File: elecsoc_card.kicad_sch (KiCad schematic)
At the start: 23 parts, among them J1 Conn_01x02_Pin, U1 NA555D

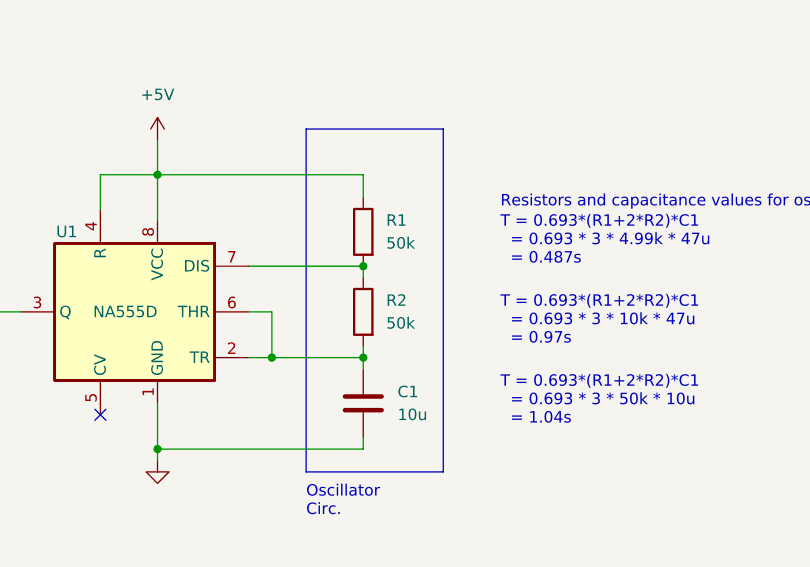
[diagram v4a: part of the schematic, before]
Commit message: Caps added and resistors changed
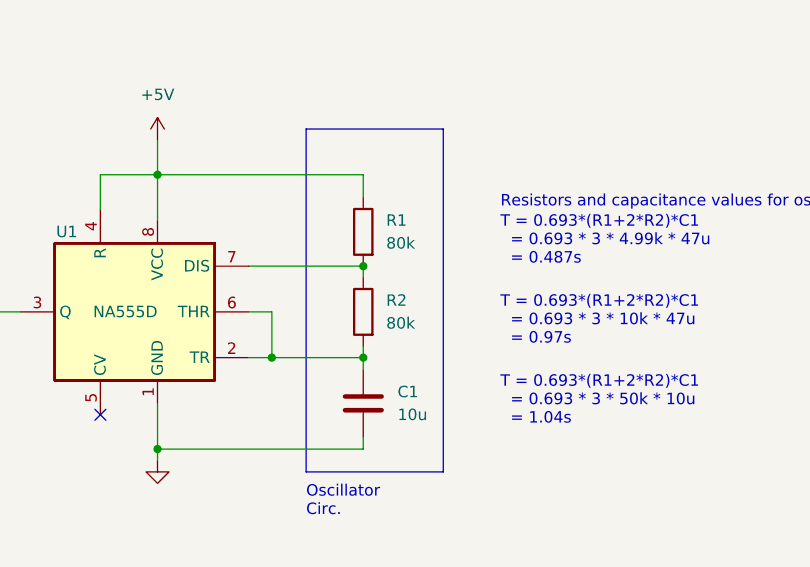
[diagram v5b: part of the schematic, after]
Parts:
- D6, D7: Mfr. No. (none) -> IN-S85AT5UW
- R1, R2: value 50k -> 80k
- U1: Mfr. No: (none) -> 621-NE555S-13
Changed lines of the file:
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@@
+      (effects (font (size 1.27 1.27)) hide)
+    )
+    (property "Mfr. No:" "621-NE555S-13" (at 156.21 91.44 0)
       (effects (font (size 1.27 1.27)) hide)
     )
@@
       (effects (font (size 1.27 1.27)) hide)
     )
-    (property "Datasheet" "~" (at 111.76 99.06 0)
+    (property "Datasheet" "https://www.mouser.ie/datasheet/2/180/IN_S85AT_Series_V1_1-2323391.pdf" (at 111.76 99.06 0)
+      (effects (font (size 1.27 1.27)) hide)
+    )
+    (property "Mfr. No." "IN-S85AT5UW" (at 111.76 99.06 90)
       (effects (font (size 1.27 1.27)) hide)
     )
@@
       (effects (font (size 1.27 1.27)) hide)
     )
-    (property "Datasheet" "~" (at 102.87 99.06 0)
+    (property "Datasheet" "https://www.mouser.ie/datasheet/2/180/IN_S85AT_Series_V1_1-2323391.pdf" (at 102.87 99.06 0)
+      (effects (font (size 1.27 1.27)) hide)
+    )
+    (property "Mfr. No." "IN-S85AT5UW" (at 102.87 99.06 90)
       (effects (font (size 1.27 1.27)) hide)
     )
@@
       (effects (font (size 1.27 1.27)) hide)
     )
-    (property "Datasheet" "~" (at 191.77 38.1 0)
+    (property "Datasheet" "https://www.mouser.ie/datasheet/2/281/1/GRT155D70G106ME13_01A-3135786.pdf" (at 191.77 38.1 0)
       (effects (font (size 1.27 1.27)) hide)
     )
@@
       (effects (font (size 1.27 1.27)) hide)
     )
-    (property "Datasheet" "~" (at 181.61 101.6 0)
+    (property "Datasheet" "https://www.mouser.ie/datasheet/2/281/1/GRT155D70G106ME13_01A-3135786.pdf" (at 181.61 101.6 0)
       (effects (font (size 1.27 1.27)) hide)
     )
@@
       (effects (font (size 1.27 1.27)) (justify right))
     )
-    (property "Value" "50k" (at 184.15 92.71 0)
+    (property "Value" "80k" (at 184.15 92.71 0)
       (effects (font (size 1.27 1.27)) (justify right))
     )
@@
       (effects (font (size 1.27 1.27)) (justify right))
     )
-    (property "Value" "50k" (at 184.15 83.82 0)
-      (effects (font (size 1.27 1.27)) (justify right))
-    )
+    (property "Value" "80k" (at 184.15 83.82 0)
+      (effects (font (size 1.27 1.27)) (justify right))
+    )

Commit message: Changed resistors
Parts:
- D1, D2, D3, D5: Mfr. No. (none) -> SMLMN2WB1CW1
- D4: Mfr. No (none) -> SMLMN2WB1CW1
- R3, R4, R5, R6, R7: value 390 -> 3k
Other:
- note added: "RED Leds Vf = 3V If = 5mA Rled = (Vs - Vf)/If = (5 - 3)/0.005 = 400 White Leds Vf = 2.9 If = 5m Rled = (Vs - Vf)/If = (5 - 2.9)/0.005 = 420"
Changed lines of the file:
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@@
+    (effects (font (size 1.27 1.27)) (justify left bottom))
+  )
+  (text "RED Leds\nVf = 3V\nIf = 5mA\nRled = (Vs - Vf)/If = (5 - 3)/0.005 = 400\n\nWhite Leds\nVf = 2.9\nIf = 5m\nRled = (Vs - Vf)/If = (5 - 2.9)/0.005 = 420"
+    (at 195.58 124.46 0)
     (effects (font (size 1.27 1.27)) (justify left bottom))
   )
@@
   )
   (symbol (lib_id "Device:R") (at 120.65 71.12 0) (mirror y) (unit 1)
-    (in_bom yes) (on_board yes) (dnp no) (fields_autoplaced)
-    (property "Reference" "R3" (at 118.11 70.485 0)
-      (effects (font (size 1.27 1.27)) (justify left))
-    )
-    (property "Value" "390" (at 118.11 73.025 0)
+    (in_bom yes) (on_board yes) (dnp no)
+    (property "Reference" "R3" (at 115.57 69.85 0)
+      (effects (font (size 1.27 1.27)) (justify right))
+    )
+    (property "Value" "3k" (at 118.11 73.025 0) (do_not_autoplace)
       (effects (font (size 1.27 1.27)) (justify left))
     )
@@
     )
     (property "Datasheet" "~" (at 111.76 82.55 0)
+      (effects (font (size 1.27 1.27)) hide)
+    )
+    (property "Mfr. No." "SMLMN2WB1CW1 " (at 111.76 82.55 90)
       (effects (font (size 1.27 1.27)) hide)
     )
@@
   )
   (symbol (lib_id "Device:R") (at 102.87 71.12 0) (mirror y) (unit 1)
-    (in_bom yes) (on_board yes) (dnp no) (fields_autoplaced)
-    (property "Reference" "R5" (at 100.33 70.485 0)
-      (effects (font (size 1.27 1.27)) (justify left))
-    )
-    (property "Value" "390" (at 100.33 73.025 0)
+    (in_bom yes) (on_board yes) (dnp no)
+    (property "Reference" "R5" (at 97.79 69.85 0)
+      (effects (font (size 1.27 1.27)) (justify right))
+    )
+    (property "Value" "3k" (at 100.33 73.025 0) (do_not_autoplace)
       (effects (font (size 1.27 1.27)) (justify left))
     )
@@
       (effects (font (size 1.27 1.27)) hide)
     )
+    (property "Mfr. No." "SMLMN2WB1CW1 " (at 120.65 82.55 90)
+      (effects (font (size 1.27 1.27)) hide)
+    )
     (pin "1")
     (pin "2")
@@
   )
   (symbol (lib_id "Device:R") (at 93.98 71.12 0) (mirror y) (unit 1)
-    (in_bom yes) (on_board yes) (dnp no) (fields_autoplaced)
-    (property "Reference" "R6" (at 91.44 70.485 0)
-      (effects (font (size 1.27 1.27)) (justify left))
-    )
-    (property "Value" "390" (at 91.44 73.025 0)
+    (in_bom yes) (on_board yes) (dnp no)
+    (property "Reference" "R6" (at 88.9 69.85 0)
+      (effects (font (size 1.27 1.27)) (justify right))
+    )
+    (property "Value" "3k" (at 91.44 73.025 0) (do_not_autoplace)
       (effects (font (size 1.27 1.27)) (justify left))
     )
@@
       (effects (font (size 1.27 1.27)) hide)
     )
+    (property "Mfr. No" "SMLMN2WB1CW1 " (at 93.98 82.55 90)
+      (effects (font (size 1.27 1.27)) hide)
+    )
     (pin "1")
     (pin "2")
@@
       (effects (font (size 1.27 1.27)) hide)
     )
+    (property "Mfr. No." "SMLMN2WB1CW1 " (at 102.87 82.55 90)
+      (effects (font (size 1.27 1.27)) hide)
+    )
     (pin "1")
     (pin "2")
@@
   )
   (symbol (lib_id "Device:R") (at 85.09 71.12 0) (mirror y) (unit 1)
-    (in_bom yes) (on_board yes) (dnp no) (fields_autoplaced)
+    (in_bom yes) (on_board yes) (dnp no)
     (property "Reference" "R7" (at 82.55 70.485 0)
       (effects (font (size 1.27 1.27)) (justify left))
     )
-    (property "Value" "390" (at 82.55 73.025 0)
+    (property "Value" "3k" (at 82.55 73.025 0) (do_not_autoplace)
       (effects (font (size 1.27 1.27)) (justify left))
     )
@@
   )
   (symbol (lib_id "Device:R") (at 111.76 71.12 0) (mirror y) (unit 1)
-    (in_bom yes) (on_board yes) (dnp no) (fields_autoplaced)
-    (property "Reference" "R4" (at 109.22 70.485 0)
-      (effects (font (size 1.27 1.27)) (justify left))
-    )
-    (property "Value" "390" (at 109.22 73.025 0)
+    (in_bom yes) (on_board yes) (dnp no)
+    (property "Reference" "R4" (at 106.68 69.85 0)
+      (effects (font (size 1.27 1.27)) (justify right))
+    )
+    (property "Value" "3k" (at 109.22 73.025 0) (do_not_autoplace)
       (effects (font (size 1.27 1.27)) (justify left))
     )
@@
       (effects (font (size 1.27 1.27)) hide)
     )
+    (property "Mfr. No." "SMLMN2WB1CW1 " (at 85.09 82.55 90)
+      (effects (font (size 1.27 1.27)) hide)
+    )

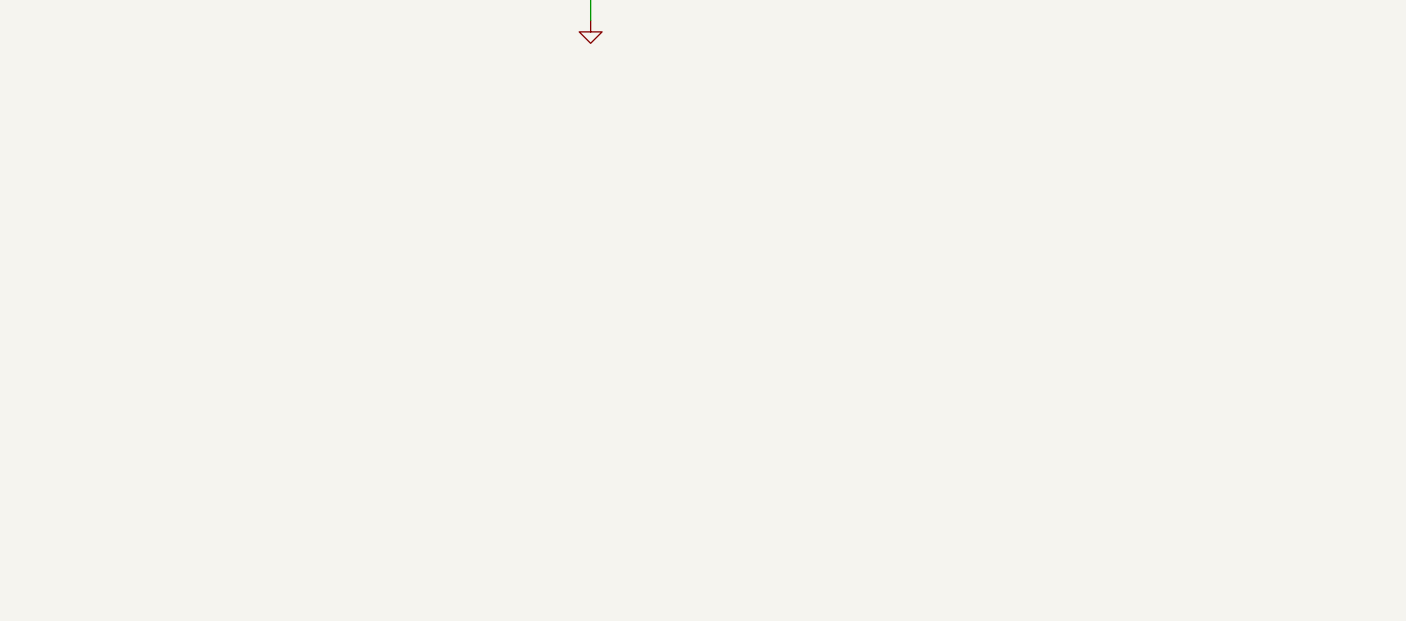
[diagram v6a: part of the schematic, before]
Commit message: Added extra resistors for soldering practice
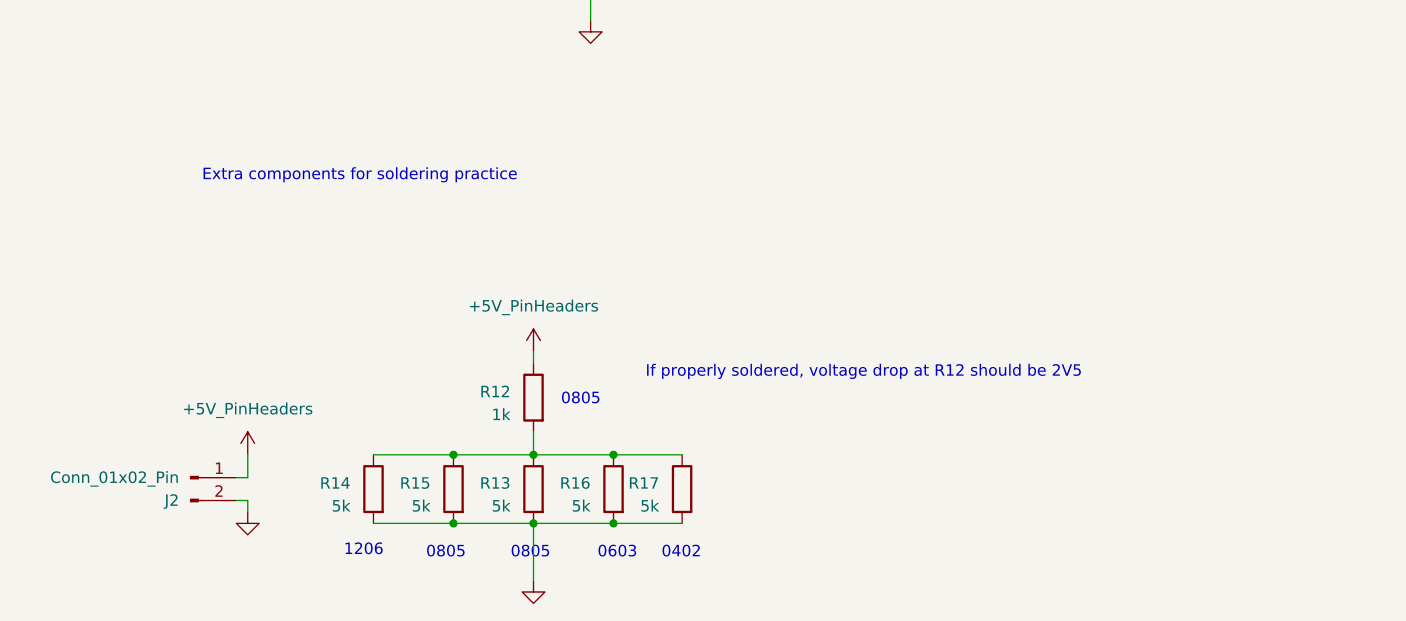
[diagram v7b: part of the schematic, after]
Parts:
- added J2: Conn_01x02_Pin, Connector_PinHeader_2.54mm:PinHeader_2x01_P2.54mm_Vertical, symbol Connector:Conn_01x02_Pin
- added R12: 1k, Resistor_SMD:R_0805_2012Metric_Pad1.20x1.40mm_HandSolder, symbol Device:R
- added R13, R15, R16, R17: 5k, Resistor_SMD:R_0805_2012Metric_Pad1.20x1.40mm_HandSolder, symbol Device:R
- added R14: 5k, Resistor_SMD:R_1206_3216Metric, symbol Device:R
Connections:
- net GND: now also J2.2 (Pin_2), R13.2, R14.2, R15.2, R16.2, R17.2
- new net: R12.2, R13.1, R14.1, R15.1, R16.1, R17.1
- new net +5V_PinHeaders: J2.1 (Pin_1), R12.1
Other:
- note added: "0402"
- note added: "0603"
- note added: "0805"
- note added: "1206"
- note added: "Extra components for soldering practice"
- note added: "If properly soldered, voltage drop at R12 should be 2V5"
